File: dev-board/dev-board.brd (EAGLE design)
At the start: 49.2 x 64.8 mm, 38 parts, among them J1 12401832E402A, U1 STM32F103RET6, U2 AT24C64BN-10SU-2.7, U3 FT232RL, U4 MCP2551, U5 LM1117IMP-3.3, X1 8MHz

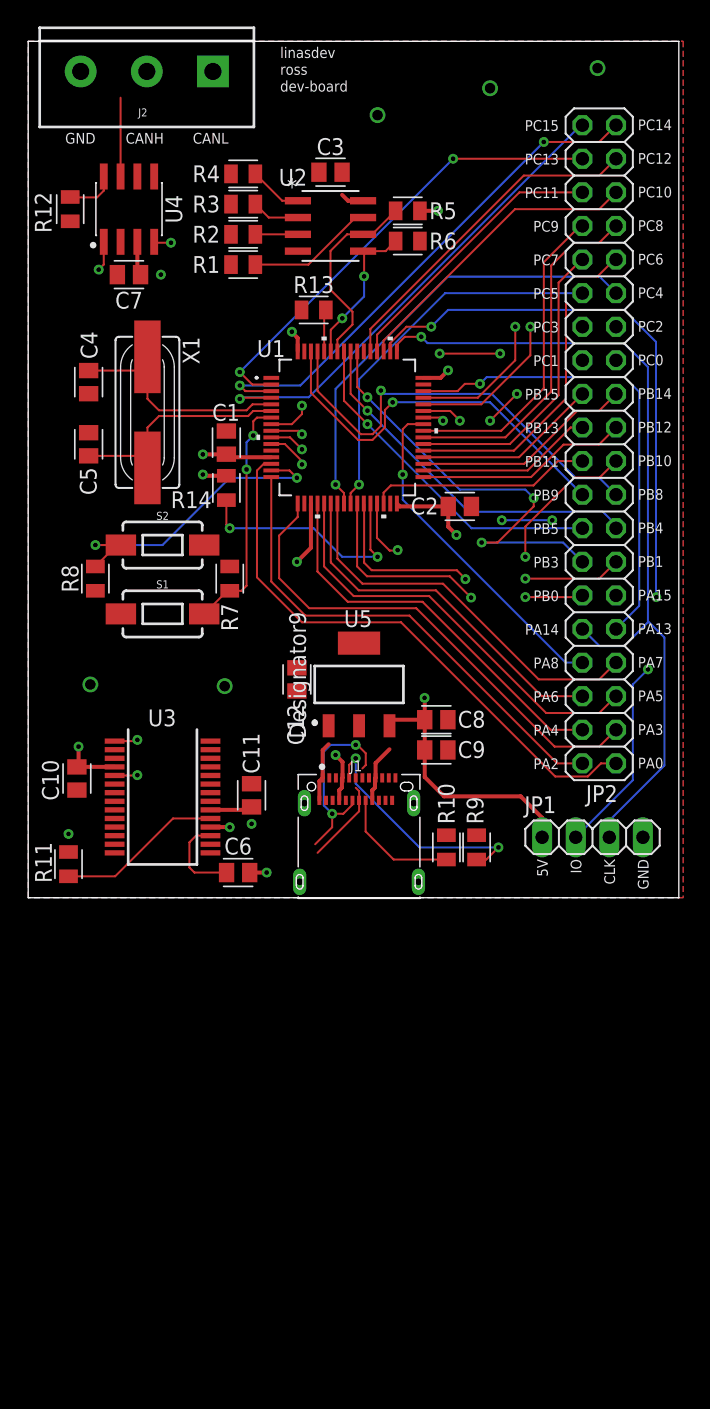
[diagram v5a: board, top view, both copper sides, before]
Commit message: Proper decoupling caps for stm32
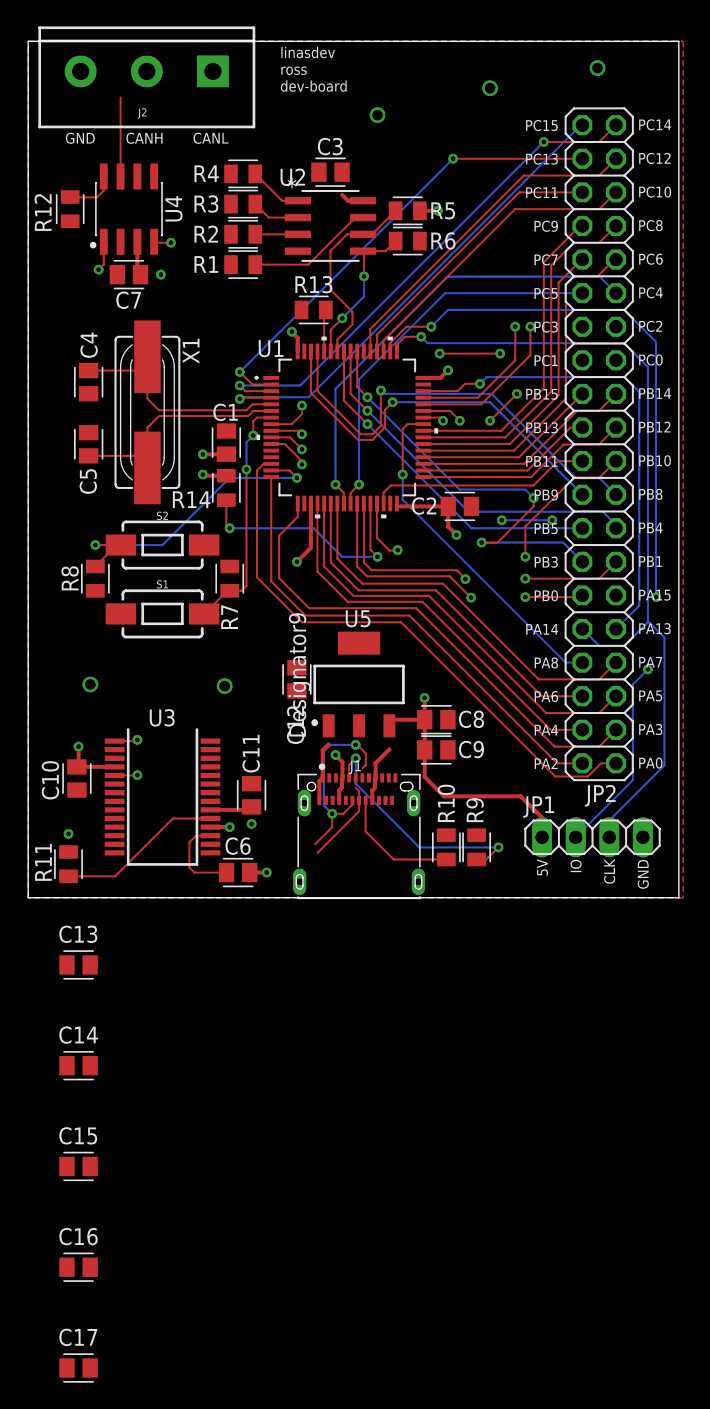
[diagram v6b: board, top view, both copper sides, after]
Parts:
- added C13, C14: 100nF, Capacitor:CAPC2012X110
- added C15: 10nF, Capacitor:CAPC2012X110
- added C16: 1uF, Capacitor:CAPC2012X110
- added C17: 4.7uF, Capacitor:CAPC2012X110
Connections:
- removed net VBAT: U1.1
- net +3V3: now also C13.1, C14.1, C15.1, C16.1, C17.1, U1.1
- net GND: now also C13.2, C14.2, C15.2, C16.2, C17.2
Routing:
- net +3V3: track 28.2 -> 24.7 mm

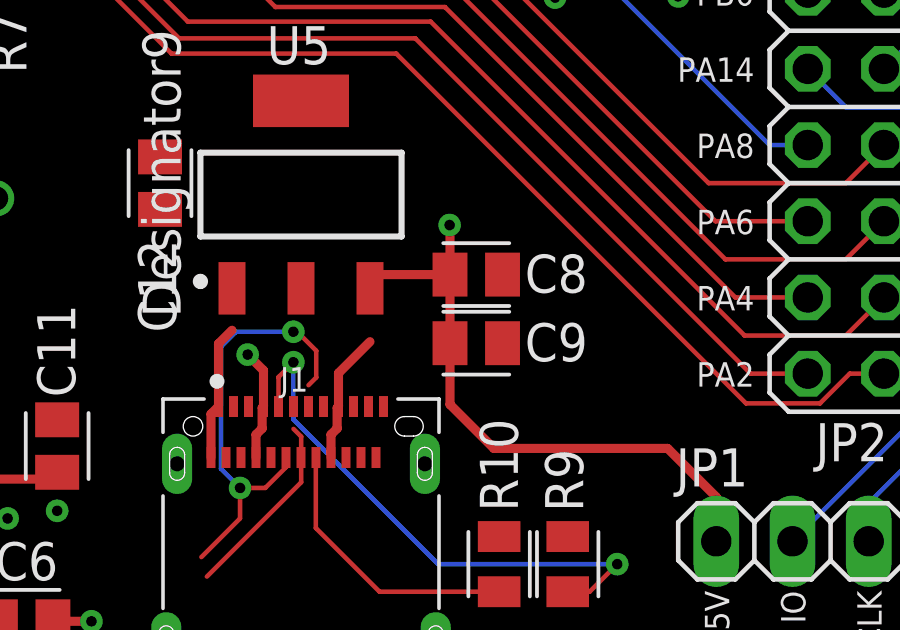
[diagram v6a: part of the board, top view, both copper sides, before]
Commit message: Proper bulk cap for regulator
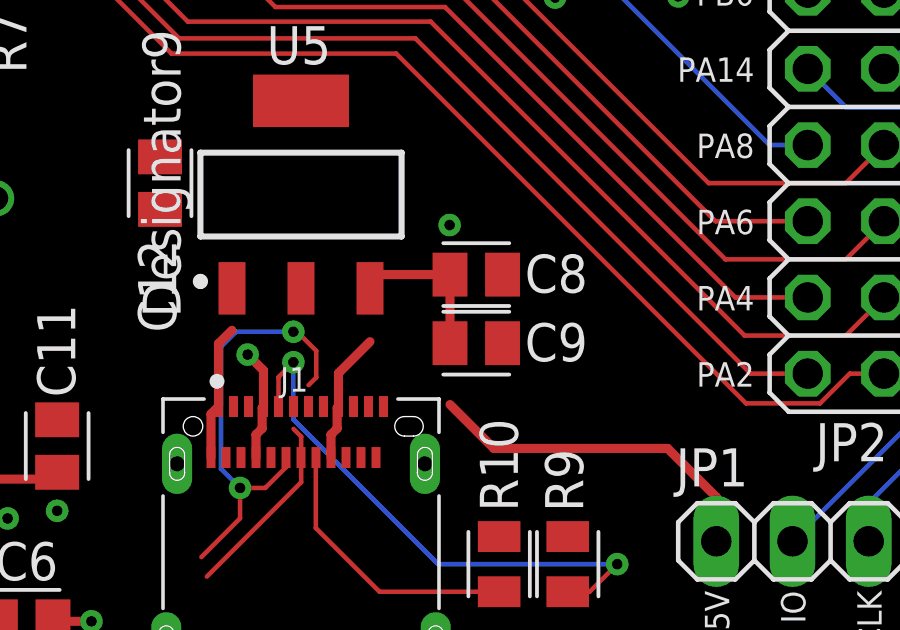
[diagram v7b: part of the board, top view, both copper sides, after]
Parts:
- C12: value 100nF -> 10uF
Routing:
- net +5V: track 114.0 -> 110.4 mm
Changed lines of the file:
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@@
 <attribute name="VOLTAGE_RATING" value="" x="52.451" y="36.957" size="1.778" layer="27" rot="R90" display="off"/>
 </element>
-<element name="C12" library="Capacitor" library_urn="urn:adsk.eagle:library:16290819" package="CAPC2012X110" package3d_urn="urn:adsk.eagle:package:16290897/2" value="100nF" x="17.78" y="16.51" smashed="yes" rot="R270">
+<element name="C12" library="Capacitor" library_urn="urn:adsk.eagle:library:16290819" package="CAPC2012X110" package3d_urn="urn:adsk.eagle:package:16290897/2" value="10uF" x="17.78" y="16.51" smashed="yes" rot="R270">
 <attribute name="CATEGORY" value="Capacitor" x="-20.32" y="-19.05" size="1.778" layer="27" rot="R270" display="off"/>
 <attribute name="MANUFACTURER" value="" x="-20.32" y="-19.05" size="1.778" layer="27" rot="R270" display="off"/>
@@
 <contactref element="J1" pad="B9"/>
 <contactref element="J1" pad="B4"/>
-<contactref element="C8" pad="1"/>
-<contactref element="C9" pad="1"/>
 <wire x1="20.979" y1="7.364" x2="20.979" y2="8.12895" width="0.3048" layer="1"/>
 <wire x1="23.479" y1="7.364" x2="23.479" y2="8.12895" width="0.3048" layer="1"/>
@@
 <wire x1="23.729" y1="9.064" x2="23.729" y2="10.176" width="0.3048" layer="1"/>
 <wire x1="24.779" y1="11.226" x2="23.729" y2="10.176" width="0.3048" layer="1"/>
-<wire x1="27.4456" y1="11.176" x2="27.4456" y2="13.462" width="0.3048" layer="1"/>
-<wire x1="27.4456" y1="13.462" x2="24.856" y2="13.462" width="0.3048" layer="1"/>
-<wire x1="24.856" y1="13.462" x2="24.779" y2="13.385" width="0.3048" layer="1"/>
 <wire x1="21.229" y1="9.064" x2="21.229" y2="10.267" width="0.3048" layer="1"/>
 <wire x1="21.229" y1="10.267" x2="20.701" y2="10.795" width="0.3048" layer="1"/>
@@
 <via x="20.701" y="10.795" extent="1-16" drill="0.35"/>
 <via x="14.351" y="5.588" extent="1-16" drill="0.35"/>
-<wire x1="27.4456" y1="13.462" x2="27.4456" y2="15.0994" width="0.3048" layer="1"/>
 <wire x1="27.4456" y1="15.0994" x2="27.432" y2="15.113" width="0.3048" layer="1"/>
 <via x="27.432" y="15.113" extent="1-16" drill="0.35"/>
@@
 <wire x1="-1.27" y1="6.604" x2="-1.27" y2="38.354" width="0.3048" layer="15"/>
 <contactref element="JP1" pad="1"/>
-<wire x1="27.4456" y1="11.176" x2="27.4456" y2="9.1304" width="0.3048" layer="1"/>
 <wire x1="27.4456" y1="9.1304" x2="28.908" y2="7.668" width="0.3048" layer="1"/>
 <wire x1="36.322" y1="4.572" x2="36.322" y2="6.0459125" width="0.3048" layer="1"/>
@@
 <contactref element="C7" pad="1"/>
 <wire x1="5.715" y1="49.6007" x2="5.715" y2="47.3574" width="0.3048" layer="1"/>
+<contactref element="C8" pad="1"/>
+<contactref element="C9" pad="1"/>
+<wire x1="27.4456" y1="11.176" x2="27.4456" y2="13.462" width="0.3048" layer="1"/>
+<wire x1="27.4456" y1="13.462" x2="24.856" y2="13.462" width="0.3048" layer="1"/>
+<wire x1="24.856" y1="13.462" x2="24.779" y2="13.385" width="0.3048" layer="1"/>
 <contactref element="U5" pad="3"/>
 <wire x1="5.715" y1="47.3574" x2="5.9554" y2="47.117" width="0" layer="19" extent="1-1"/>
 <wire x1="7.493" y1="47.117" x2="5.9554" y2="47.117" width="0" layer="19" extent="1-1"/>
-<wire x1="24.779" y1="13.004" x2="24.779" y2="13.385" width="0" layer="19" extent="1-1"/>
 <wire x1="14.1244" y1="6.645" x2="14.351" y2="5.588" width="0" layer="19" extent="1-1"/>
 <wire x1="14.351" y1="6.8716" x2="14.1244" y2="6.645" width="0" layer="19" extent="1-1"/>
 <wire x1="0.508" y1="3.4595" x2="0.508" y2="4.826" width="0" layer="19" extent="1-1"/>
+<wire x1="27.4456" y1="13.462" x2="27.4456" y2="15.0994" width="0" layer="19" extent="1-1"/>
+<wire x1="24.779" y1="13.004" x2="24.779" y2="13.385" width="0" layer="19" extent="1-1"/>
 <wire x1="24.779" y1="11.226" x2="24.779" y2="13.004" width="0" layer="19" extent="1-1"/>
+<wire x1="27.4456" y1="9.1304" x2="27.4456" y2="11.176" width="0" layer="19" extent="1-1"/>
 </signal>
 <signal name="GND">
@@
 <contactref element="R9" pad="1"/>
 <contactref element="R10" pad="2"/>
-<contactref element="C8" pad="2"/>
-<contactref element="C9" pad="2"/>
 <contactref element="R12" pad="1"/>
 <contactref element="R14" pad="1"/>
@@
 <contactref element="C15" pad="2"/>
 <contactref element="C17" pad="2"/>
+<contactref element="C8" pad="2"/>
+<contactref element="C9" pad="2"/>
 <wire x1="32.385" y1="61.214" x2="40.513" y2="62.738" width="0" layer="19" extent="1-1"/>
 <wire x1="23.876" y1="59.182" x2="32.385" y2="61.214" width="0" layer="19" extent="1-1"/>

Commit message: Bulkier MCP2551 decoupling cap
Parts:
- C7: value 100nF -> 4.7uF
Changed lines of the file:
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@@
 <attribute name="VOLTAGE_RATING" value="" x="-40.005" y="31.115" size="1.778" layer="27" rot="R180" display="off"/>
 </element>
-<element name="C7" library="Capacitor" library_urn="urn:adsk.eagle:library:16290819" package="CAPC2012X110" package3d_urn="urn:adsk.eagle:package:16290897/2" value="100nF" x="5.08" y="47.117" smashed="yes" rot="R180">
+<element name="C7" library="Capacitor" library_urn="urn:adsk.eagle:library:16290819" package="CAPC2012X110" package3d_urn="urn:adsk.eagle:package:16290897/2" value="4.7uF" x="5.08" y="47.117" smashed="yes" rot="R180">
 <attribute name="CATEGORY" value="Capacitor" x="-54.61" y="76.327" size="1.778" layer="27" rot="R180" display="off"/>
 <attribute name="MANUFACTURER" value="" x="-54.61" y="76.327" size="1.778" layer="27" rot="R180" display="off"/>
